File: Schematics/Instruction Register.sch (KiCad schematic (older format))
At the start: 44 parts, among them U46 74F157, U47 74F157, U48 74F574, U49 74F157, U50 74F157, U51 74F574

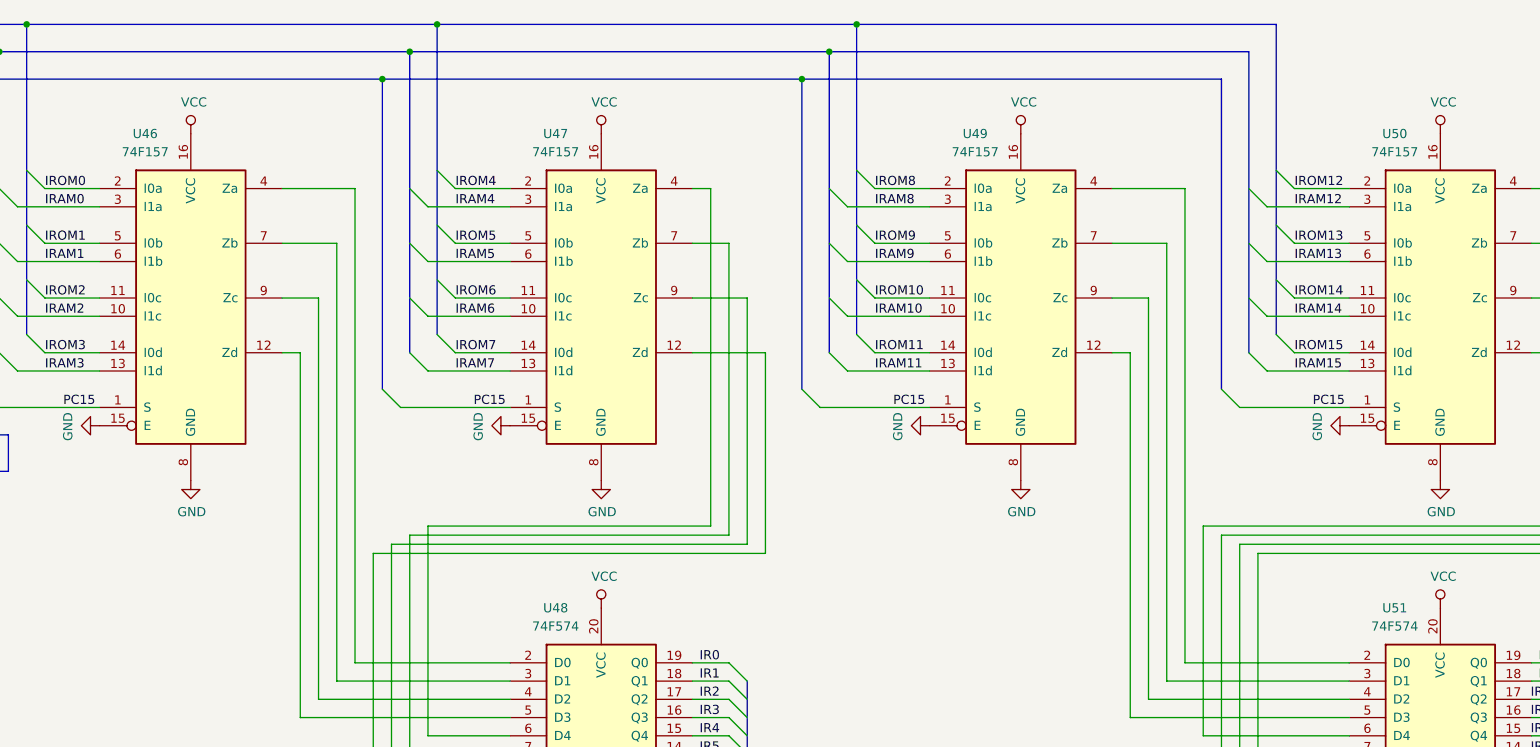
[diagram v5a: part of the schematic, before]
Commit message: Add unused IC units to Output Display to ensure no ICs are shared with other modules.
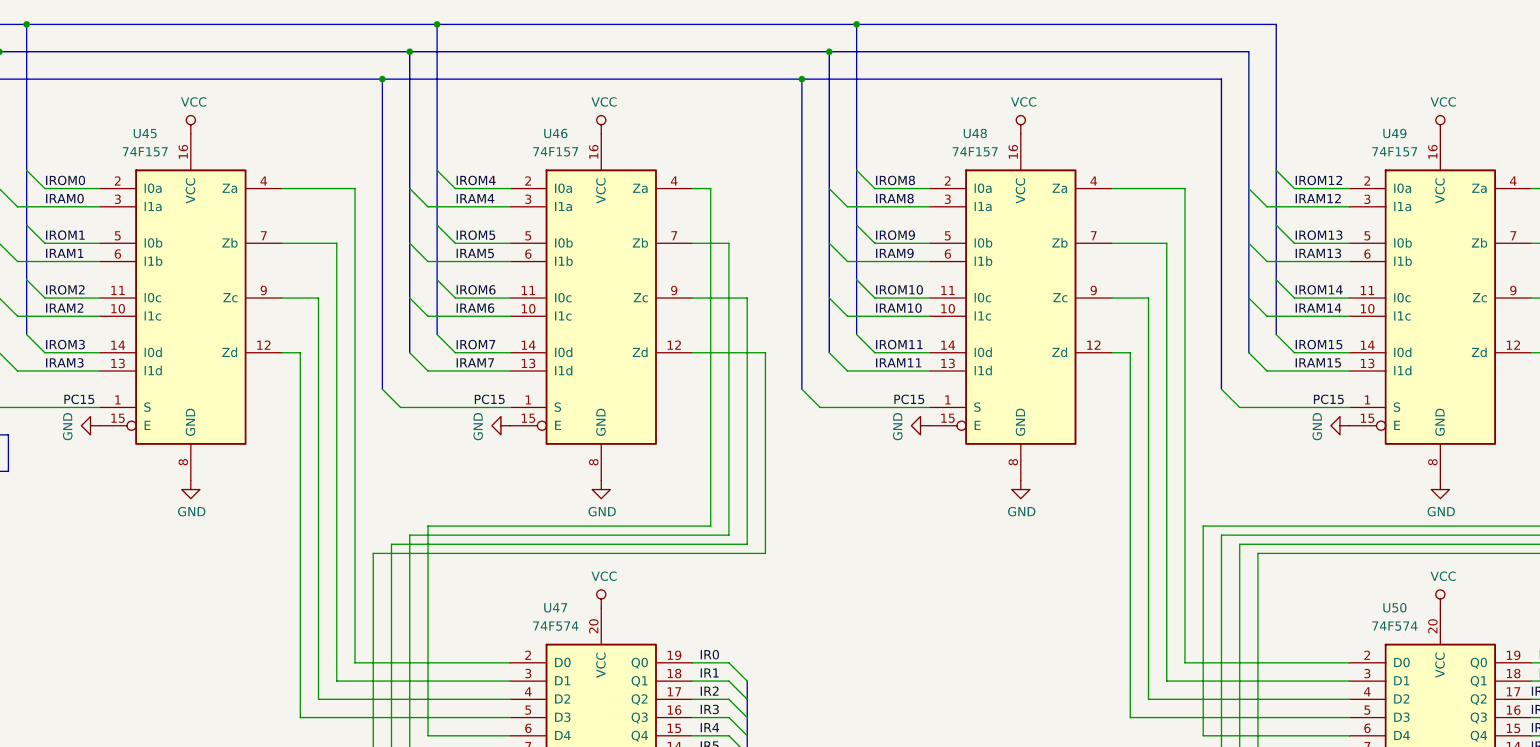
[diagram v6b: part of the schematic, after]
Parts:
- renumbered U46 to U45, U47 to U46, U48 to U47, U49 to U48, U50 to U49, U51 to U50
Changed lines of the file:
@@
 P 2100 2100
 AR Path="/5D2C14C3/5D23E2DA" Ref="U?"  Part="1"
-AR Path="/5D8005AF/5D833E49/5D23E2DA" Ref="U46"  Part="1"
-F 0 "U46" H 1850 3000 50  0000 C CNN
+AR Path="/5D8005AF/5D833E49/5D23E2DA" Ref="U45"  Part="1"
+F 0 "U45" H 1850 3000 50  0000 C CNN
 F 1 "74F157" H 1850 2900 50  0000 C CNN
 F 2 "Package_DIP:DIP-16_W7.62mm" H 2100 2100 50  0001 C CNN
@@
 P 4350 4600
 AR Path="/5D2C14C3/5D25C885" Ref="U?"  Part="1"
-AR Path="/5D8005AF/5D833E49/5D25C885" Ref="U48"  Part="1"
-F 0 "U48" H 4100 5400 50  0000 C CNN
+AR Path="/5D8005AF/5D833E49/5D25C885" Ref="U47"  Part="1"
+F 0 "U47" H 4100 5400 50  0000 C CNN
 F 1 "74F574" H 4100 5300 50  0000 C CNN
 F 2 "Package_DIP:DIP-20_W7.62mm" H 4350 4600 50  0001 C CNN
@@
 P 8950 4600
 AR Path="/5D2C14C3/5D26023C" Ref="U?"  Part="1"
-AR Path="/5D8005AF/5D833E49/5D26023C" Ref="U51"  Part="1"
-F 0 "U51" H 8700 5400 50  0000 C CNN
+AR Path="/5D8005AF/5D833E49/5D26023C" Ref="U50"  Part="1"
+F 0 "U50" H 8700 5400 50  0000 C CNN
 F 1 "74F574" H 8700 5300 50  0000 C CNN
 F 2 "Package_DIP:DIP-20_W7.62mm" H 8950 4600 50  0001 C CNN
@@
 P 2100 3100
 AR Path="/5D2C14C3/5D268258" Ref="#PWR?"  Part="1"
-AR Path="/5D8005AF/5D833E49/5D268258" Ref="#PWR0192"  Part="1"
-F 0 "#PWR0192" H 2100 2850 50  0001 C CNN
+AR Path="/5D8005AF/5D833E49/5D268258" Ref="#PWR097"  Part="1"
+F 0 "#PWR097" H 2100 2850 50  0001 C CNN
 F 1 "GND" H 2105 2927 50  0000 C CNN
 F 2 "" H 2100 3100 50  0001 C CNN
@@
 P 4350 5400
 AR Path="/5D2C14C3/5D930BD4" Ref="#PWR?"  Part="1"
-AR Path="/5D8005AF/5D833E49/5D930BD4" Ref="#PWR0193"  Part="1"
-F 0 "#PWR0193" H 4350 5150 50  0001 C CNN
+AR Path="/5D8005AF/5D833E49/5D930BD4" Ref="#PWR0103"  Part="1"
+F 0 "#PWR0103" H 4350 5150 50  0001 C CNN
 F 1 "GND" H 4355 5227 50  0000 C CNN
 F 2 "" H 4350 5400 50  0001 C CNN
@@
 P 8950 5400
 AR Path="/5D2C14C3/5D930FC4" Ref="#PWR?"  Part="1"
-AR Path="/5D8005AF/5D833E49/5D930FC4" Ref="#PWR0194"  Part="1"
-F 0 "#PWR0194" H 8950 5150 50  0001 C CNN
+AR Path="/5D8005AF/5D833E49/5D930FC4" Ref="#PWR0112"  Part="1"
+F 0 "#PWR0112" H 8950 5150 50  0001 C CNN
 F 1 "GND" H 8955 5227 50  0000 C CNN
 F 2 "" H 8950 5400 50  0001 C CNN
@@
 P 3850 5100
 AR Path="/5D2C14C3/5D93F174" Ref="#PWR?"  Part="1"
-AR Path="/5D8005AF/5D833E49/5D93F174" Ref="#PWR0195"  Part="1"
-F 0 "#PWR0195" H 3850 4850 50  0001 C CNN
+AR Path="/5D8005AF/5D833E49/5D93F174" Ref="#PWR099"  Part="1"
+F 0 "#PWR099" H 3850 4850 50  0001 C CNN
 F 1 "GND" H 3855 4927 50  0000 C CNN
 F 2 "" H 3850 5100 50  0001 C CNN
@@
 P 8450 5100
 AR Path="/5D2C14C3/5D944146" Ref="#PWR?"  Part="1"
-AR Path="/5D8005AF/5D833E49/5D944146" Ref="#PWR0196"  Part="1"
-F 0 "#PWR0196" H 8450 4850 50  0001 C CNN
+AR Path="/5D8005AF/5D833E49/5D944146" Ref="#PWR0108"  Part="1"
+F 0 "#PWR0108" H 8450 4850 50  0001 C CNN
 F 1 "GND" H 8455 4927 50  0000 C CNN
 F 2 "" H 8450 5100 50  0001 C CNN
@@
 P 8950 3800
 AR Path="/5D2C14C3/5D9520FE" Ref="#PWR?"  Part="1"
-AR Path="/5D8005AF/5D833E49/5D9520FE" Ref="#PWR0197"  Part="1"
-F 0 "#PWR0197" H 8950 3650 50  0001 C CNN
+AR Path="/5D8005AF/5D833E49/5D9520FE" Ref="#PWR0111"  Part="1"
+F 0 "#PWR0111" H 8950 3650 50  0001 C CNN
 F 1 "VCC" H 8967 3973 50  0000 C CNN
 F 2 "" H 8950 3800 50  0001 C CNN
@@
 P 2100 1200
 AR Path="/5D2C14C3/5D956349" Ref="#PWR?"  Part="1"
-AR Path="/5D8005AF/5D833E49/5D956349" Ref="#PWR0198"  Part="1"
-F 0 "#PWR0198" H 2100 1050 50  0001 C CNN
+AR Path="/5D8005AF/5D833E49/5D956349" Ref="#PWR096"  Part="1"
+F 0 "#PWR096" H 2100 1050 50  0001 C CNN
 F 1 "VCC" H 2117 1373 50  0000 C CNN
 F 2 "" H 2100 1200 50  0001 C CNN
@@
 P 4350 1200
 AR Path="/5D2C14C3/5D956707" Ref="#PWR?"  Part="1"
-AR Path="/5D8005AF/5D833E49/5D956707" Ref="#PWR0199"  Part="1"
-F 0 "#PWR0199" H 4350 1050 50  0001 C CNN
+AR Path="/5D8005AF/5D833E49/5D956707" Ref="#PWR0100"  Part="1"
+F 0 "#PWR0100" H 4350 1050 50  0001 C CNN
 F 1 "VCC" H 4367 1373 50  0000 C CNN
 F 2 "" H 4350 1200 50  0001 C CNN
@@
 P 4350 3800
 AR Path="/5D2C14C3/5D95761A" Ref="#PWR?"  Part="1"
-AR Path="/5D8005AF/5D833E49/5D95761A" Ref="#PWR0200"  Part="1"
-F 0 "#PWR0200" H 4350 3650 50  0001 C CNN
+AR Path="/5D8005AF/5D833E49/5D95761A" Ref="#PWR0102"  Part="1"
+F 0 "#PWR0102" H 4350 3650 50  0001 C CNN
 F 1 "VCC" H 4367 3973 50  0000 C CNN
 F 2 "" H 4350 3800 50  0001 C CNN
@@
 P 1600 2800
 AR Path="/5D2C14C3/5D966870" Ref="#PWR?"  Part="1"
-AR Path="/5D8005AF/5D833E49/5D966870" Ref="#PWR0201"  Part="1"
-F 0 "#PWR0201" H 1600 2550 50  0001 C CNN
+AR Path="/5D8005AF/5D833E49/5D966870" Ref="#PWR093"  Part="1"
+F 0 "#PWR093" H 1600 2550 50  0001 C CNN
 F 1 "GND" H 1605 2627 50  0000 C CNN
 F 2 "" H 1600 2800 50  0001 C CNN
@@
 P 3850 2800
 AR Path="/5D2C14C3/5D972255" Ref="#PWR?"  Part="1"
-AR Path="/5D8005AF/5D833E49/5D972255" Ref="#PWR0202"  Part="1"
-F 0 "#PWR0202" H 3850 2550 50  0001 C CNN
+AR Path="/5D8005AF/5D833E49/5D972255" Ref="#PWR098"  Part="1"
+F 0 "#PWR098" H 3850 2550 50  0001 C CNN
 F 1 "GND" H 3855 2627 50  0000 C CNN
 F 2 "" H 3850 2800 50  0001 C CNN
@@
 P 4350 3100
 AR Path="/5D2C14C3/5D97CF13" Ref="#PWR?"  Part="1"
-AR Path="/5D8005AF/5D833E49/5D97CF13" Ref="#PWR0203"  Part="1"
-F 0 "#PWR0203" H 4350 2850 50  0001 C CNN
+AR Path="/5D8005AF/5D833E49/5D97CF13" Ref="#PWR0101"  Part="1"
+F 0 "#PWR0101" H 4350 2850 50  0001 C CNN
 F 1 "GND" H 4355 2927 50  0000 C CNN
 F 2 "" H 4350 3100 50  0001 C CNN
@@
 P 4350 2100
 AR Path="/5D2C14C3/5D24114A" Ref="U?"  Part="1"
-AR Path="/5D8005AF/5D833E49/5D24114A" Ref="U47"  Part="1"
-F 0 "U47" H 4100 3000 50  0000 C CNN
+AR Path="/5D8005AF/5D833E49/5D24114A" Ref="U46"  Part="1"
+F 0 "U46" H 4100 3000 50  0000 C CNN
 F 1 "74F157" H 4100 2900 50  0000 C CNN
 F 2 "Package_DIP:DIP-16_W7.62mm" H 4350 2100 50  0001 C CNN
@@
 P 6650 1200
 AR Path="/5D2C14C3/5DA1423D" Ref="#PWR?"  Part="1"
-AR Path="/5D8005AF/5D833E49/5DA1423D" Ref="#PWR0204"  Part="1"
-F 0 "#PWR0204" H 6650 1050 50  0001 C CNN
+AR Path="/5D8005AF/5D833E49/5DA1423D" Ref="#PWR0105"  Part="1"
+F 0 "#PWR0105" H 6650 1050 50  0001 C CNN
 F 1 "VCC" H 6667 1373 50  0000 C CNN
 F 2 "" H 6650 1200 50  0001 C CNN
@@
 P 6150 2800
 AR Path="/5D2C14C3/5DA14243" Ref="#PWR?"  Part="1"
-AR Path="/5D8005AF/5D833E49/5DA14243" Ref="#PWR0205"  Part="1"
-F 0 "#PWR0205" H 6150 2550 50  0001 C CNN
+AR Path="/5D8005AF/5D833E49/5DA14243" Ref="#PWR0104"  Part="1"
+F 0 "#PWR0104" H 6150 2550 50  0001 C CNN
 F 1 "GND" H 6155 2627 50  0000 C CNN
 F 2 "" H 6150 2800 50  0001 C CNN
@@
 P 6650 3100
 AR Path="/5D2C14C3/5DA14249" Ref="#PWR?"  Part="1"
-AR Path="/5D8005AF/5D833E49/5DA14249" Ref="#PWR0206"  Part="1"
-F 0 "#PWR0206" H 6650 2850 50  0001 C CNN
+AR Path="/5D8005AF/5D833E49/5DA14249" Ref="#PWR0106"  Part="1"
+F 0 "#PWR0106" H 6650 2850 50  0001 C CNN
 F 1 "GND" H 6655 2927 50  0000 C CNN
 F 2 "" H 6650 3100 50  0001 C CNN
@@
 P 6650 2100
 AR Path="/5D2C14C3/5DA1424F" Ref="U?"  Part="1"
-AR Path="/5D8005AF/5D833E49/5DA1424F" Ref="U49"  Part="1"
-F 0 "U49" H 6400 3000 50  0000 C CNN
+AR Path="/5D8005AF/5D833E49/5DA1424F" Ref="U48"  Part="1"
+F 0 "U48" H 6400 3000 50  0000 C CNN
 F 1 "74F157" H 6400 2900 50  0000 C CNN
 F 2 "Package_DIP:DIP-16_W7.62mm" H 6650 2100 50  0001 C CNN
@@
 P 8950 1200
 AR Path="/5D2C14C3/5DA1932D" Ref="#PWR?"  Part="1"
-AR Path="/5D8005AF/5D833E49/5DA1932D" Ref="#PWR0207"  Part="1"
-F 0 "#PWR0207" H 8950 1050 50  0001 C CNN
+AR Path="/5D8005AF/5D833E49/5DA1932D" Ref="#PWR0109"  Part="1"
+F 0 "#PWR0109" H 8950 1050 50  0001 C CNN
 F 1 "VCC" H 8967 1373 50  0000 C CNN
 F 2 "" H 8950 1200 50  0001 C CNN
@@
 P 8450 2800
 AR Path="/5D2C14C3/5DA19333" Ref="#PWR?"  Part="1"
-AR Path="/5D8005AF/5D833E49/5DA19333" Ref="#PWR0208"  Part="1"
-F 0 "#PWR0208" H 8450 2550 50  0001 C CNN
+AR Path="/5D8005AF/5D833E49/5DA19333" Ref="#PWR0107"  Part="1"
+F 0 "#PWR0107" H 8450 2550 50  0001 C CNN
 F 1 "GND" H 8455 2627 50  0000 C CNN
 F 2 "" H 8450 2800 50  0001 C CNN
@@
 P 8950 3100
 AR Path="/5D2C14C3/5DA19339" Ref="#PWR?"  Part="1"
-AR Path="/5D8005AF/5D833E49/5DA19339" Ref="#PWR0209"  Part="1"
-F 0 "#PWR0209" H 8950 2850 50  0001 C CNN
+AR Path="/5D8005AF/5D833E49/5DA19339" Ref="#PWR0110"  Part="1"
+F 0 "#PWR0110" H 8950 2850 50  0001 C CNN
 F 1 "GND" H 8955 2927 50  0000 C CNN
 F 2 "" H 8950 3100 50  0001 C CNN
@@
 P 8950 2100
 AR Path="/5D2C14C3/5DA1933F" Ref="U?"  Part="1"
-AR Path="/5D8005AF/5D833E49/5DA1933F" Ref="U50"  Part="1"
-F 0 "U50" H 8700 3000 50  0000 C CNN
+AR Path="/5D8005AF/5D833E49/5DA1933F" Ref="U49"  Part="1"
+F 0 "U49" H 8700 3000 50  0000 C CNN
 F 1 "74F157" H 8700 2900 50  0000 C CNN
 F 2 "Package_DIP:DIP-16_W7.62mm" H 8950 2100 50  0001 C CNN
@@
 P 1850 7600
 AR Path="/5D2C14C3/5D80B048" Ref="#PWR?"  Part="1"
-AR Path="/5D8005AF/5D833E49/5D80B048" Ref="#PWR0210"  Part="1"
-F 0 "#PWR0210" H 1850 7450 50  0001 C CNN
+AR Path="/5D8005AF/5D833E49/5D80B048" Ref="#PWR094"  Part="1"
+F 0 "#PWR094" H 1850 7450 50  0001 C CNN
 F 1 "VCC" H 1867 7773 50  0000 C CNN
 F 2 "" H 1850 7600 50  0001 C CNN
@@
 P 1850 7900
 AR Path="/5D2C14C3/5D813D3B" Ref="#PWR?"  Part="1"
-AR Path="/5D8005AF/5D833E49/5D813D3B" Ref="#PWR0211"  Part="1"
-F 0 "#PWR0211" H 1850 7650 50  0001 C CNN
+AR Path="/5D8005AF/5D833E49/5D813D3B" Ref="#PWR095"  Part="1"
+F 0 "#PWR095" H 1850 7650 50  0001 C CNN
 F 1 "GND" H 1855 7727 50  0000 C CNN
 F 2 "" H 1850 7900 50  0001 C CNN
@@
 P 900 7300
 AR Path="/5D2C14C3/5DD45DFD" Ref="#PWR?"  Part="1"
-AR Path="/5D8005AF/5D833E49/5DD45DFD" Ref="#PWR0212"  Part="1"
-F 0 "#PWR0212" H 900 7050 50  0001 C CNN
+AR Path="/5D8005AF/5D833E49/5DD45DFD" Ref="#PWR092"  Part="1"
+F 0 "#PWR092" H 900 7050 50  0001 C CNN
 F 1 "GND" H 905 7127 50  0000 C CNN
 F 2 "" H 900 7300 50  0001 C CNN

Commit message: Add unused IC units to Data RAM to ensure no ICs are shared with other modules.
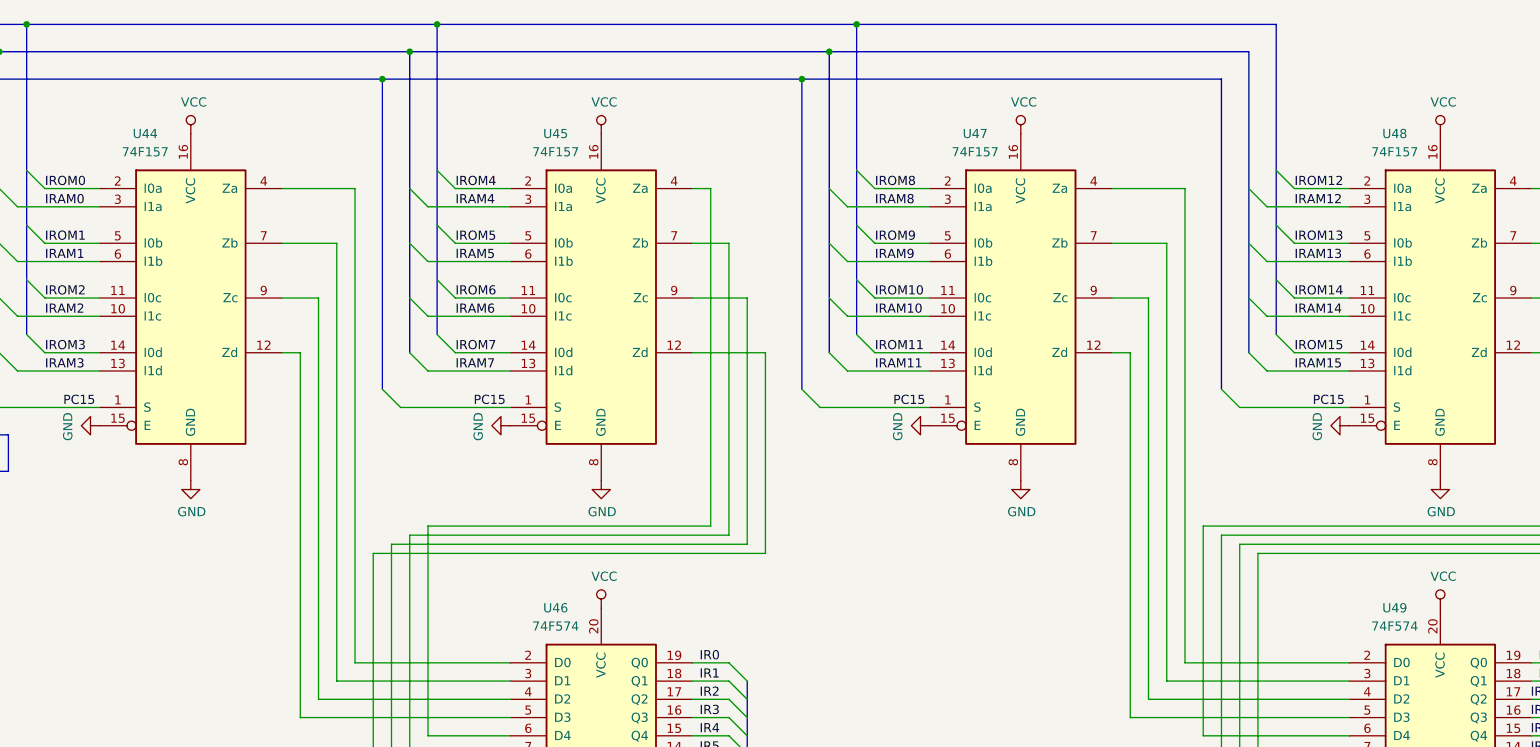
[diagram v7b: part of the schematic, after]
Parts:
- renumbered U45 to U44, U46 to U45, U47 to U46, U48 to U47, U49 to U48, U50 to U49
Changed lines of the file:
@@
 P 2100 2100
 AR Path="/5D2C14C3/5D23E2DA" Ref="U?"  Part="1"
-AR Path="/5D8005AF/5D833E49/5D23E2DA" Ref="U45"  Part="1"
-F 0 "U45" H 1850 3000 50  0000 C CNN
+AR Path="/5D8005AF/5D833E49/5D23E2DA" Ref="U44"  Part="1"
+F 0 "U44" H 1850 3000 50  0000 C CNN
 F 1 "74F157" H 1850 2900 50  0000 C CNN
 F 2 "Package_DIP:DIP-16_W7.62mm" H 2100 2100 50  0001 C CNN
@@
 P 4350 4600
 AR Path="/5D2C14C3/5D25C885" Ref="U?"  Part="1"
-AR Path="/5D8005AF/5D833E49/5D25C885" Ref="U47"  Part="1"
-F 0 "U47" H 4100 5400 50  0000 C CNN
+AR Path="/5D8005AF/5D833E49/5D25C885" Ref="U46"  Part="1"
+F 0 "U46" H 4100 5400 50  0000 C CNN
 F 1 "74F574" H 4100 5300 50  0000 C CNN
 F 2 "Package_DIP:DIP-20_W7.62mm" H 4350 4600 50  0001 C CNN
@@
 P 8950 4600
 AR Path="/5D2C14C3/5D26023C" Ref="U?"  Part="1"
-AR Path="/5D8005AF/5D833E49/5D26023C" Ref="U50"  Part="1"
-F 0 "U50" H 8700 5400 50  0000 C CNN
+AR Path="/5D8005AF/5D833E49/5D26023C" Ref="U49"  Part="1"
+F 0 "U49" H 8700 5400 50  0000 C CNN
 F 1 "74F574" H 8700 5300 50  0000 C CNN
 F 2 "Package_DIP:DIP-20_W7.62mm" H 8950 4600 50  0001 C CNN
@@
 P 4350 2100
 AR Path="/5D2C14C3/5D24114A" Ref="U?"  Part="1"
-AR Path="/5D8005AF/5D833E49/5D24114A" Ref="U46"  Part="1"
-F 0 "U46" H 4100 3000 50  0000 C CNN
+AR Path="/5D8005AF/5D833E49/5D24114A" Ref="U45"  Part="1"
+F 0 "U45" H 4100 3000 50  0000 C CNN
 F 1 "74F157" H 4100 2900 50  0000 C CNN
 F 2 "Package_DIP:DIP-16_W7.62mm" H 4350 2100 50  0001 C CNN
@@
 P 6650 2100
 AR Path="/5D2C14C3/5DA1424F" Ref="U?"  Part="1"
-AR Path="/5D8005AF/5D833E49/5DA1424F" Ref="U48"  Part="1"
-F 0 "U48" H 6400 3000 50  0000 C CNN
+AR Path="/5D8005AF/5D833E49/5DA1424F" Ref="U47"  Part="1"
+F 0 "U47" H 6400 3000 50  0000 C CNN
 F 1 "74F157" H 6400 2900 50  0000 C CNN
 F 2 "Package_DIP:DIP-16_W7.62mm" H 6650 2100 50  0001 C CNN
@@
 P 8950 2100
 AR Path="/5D2C14C3/5DA1933F" Ref="U?"  Part="1"
-AR Path="/5D8005AF/5D833E49/5DA1933F" Ref="U49"  Part="1"
-F 0 "U49" H 8700 3000 50  0000 C CNN
+AR Path="/5D8005AF/5D833E49/5DA1933F" Ref="U48"  Part="1"
+F 0 "U48" H 8700 3000 50  0000 C CNN
 F 1 "74F157" H 8700 2900 50  0000 C CNN
 F 2 "Package_DIP:DIP-16_W7.62mm" H 8950 2100 50  0001 C CNN
